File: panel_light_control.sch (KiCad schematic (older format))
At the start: 77 parts, among them J1 Conn_01x02, J6 Conn_01x04, Q1 IRF540N, Q2 IRF540N, Q3 IRF540N, U1 L7805, U2 LM324

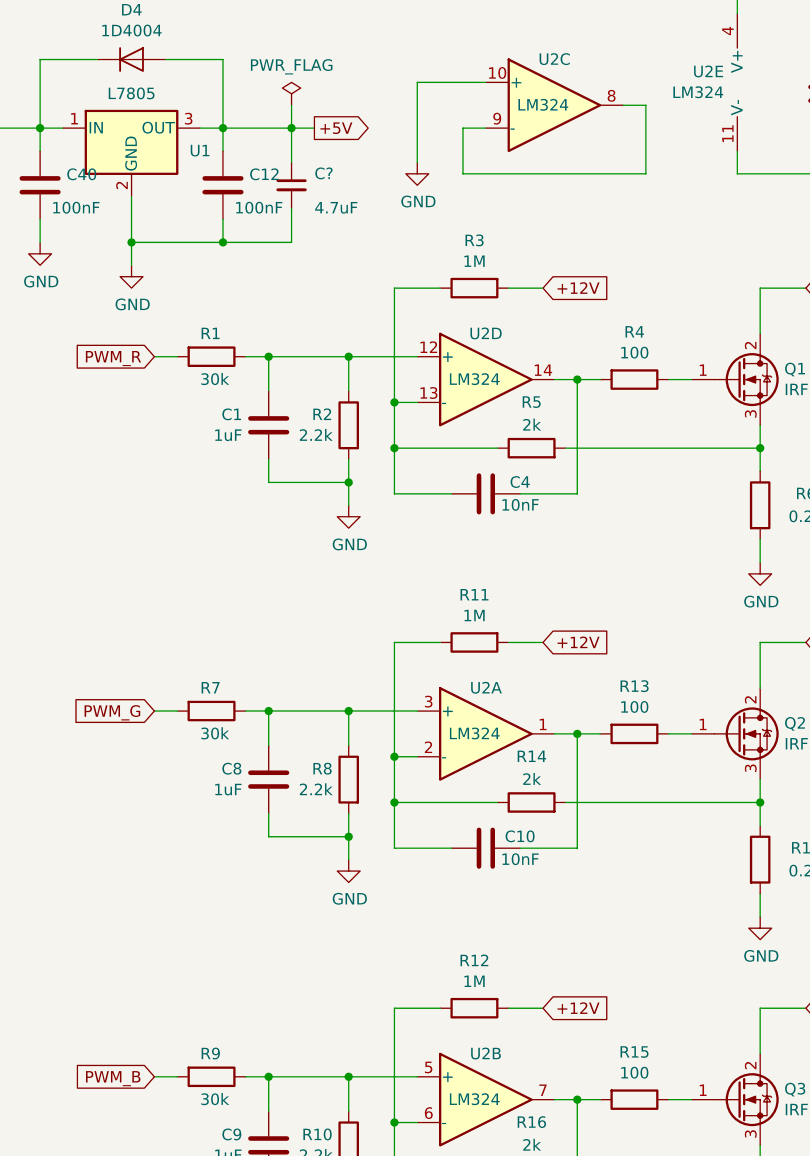
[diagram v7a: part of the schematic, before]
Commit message: added BOM info, minor tweaks to artwork
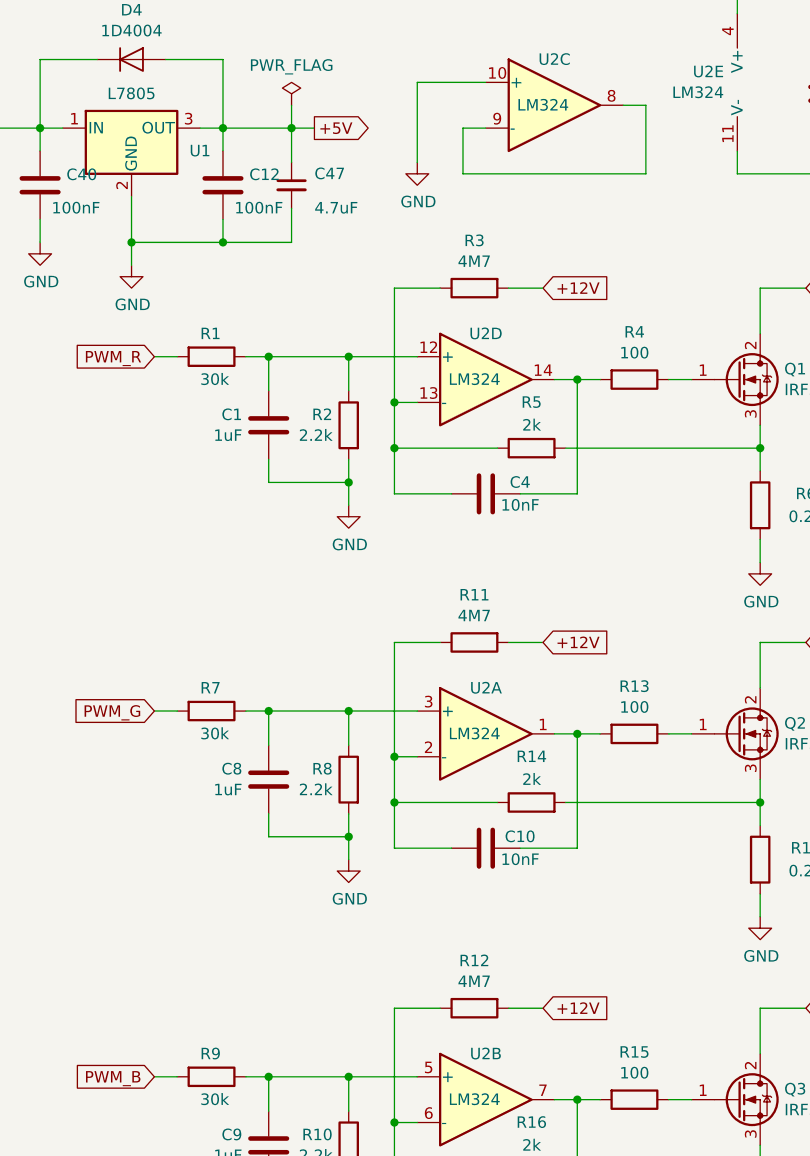
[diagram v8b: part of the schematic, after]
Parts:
- DBG1: DigiKey (none) -> 455-1723-ND‎; MPN (none) -> S6B-PH-K-S(LF)(SN)‎
- I2C1, UART1: DigiKey (none) -> 455-1721-ND‎; MPN (none) -> S4B-PH-K-S(LF)(SN)‎
- J6: DigiKey (none) -> 455-1721-ND‎; MPN (none) -> S4B-PH-K-S(LF)(SN)
- JTAG1: DigiKey (none) -> 455-1724-ND‎; MPN (none) -> S7B-PH-K-S(LF)(SN)‎
- PANEL1, PANEL2: MPN (none) -> PJ-063AH; Mouser (none) -> 490-PJ-063AH
- PS1, PS2: Mouser (none) -> 709-LDD-1000H
- Q1, Q2, Q3: MPN (none) -> IRF540NPBF; Mouser (none) -> 942-IRF540NPBF
- R11, R12, R3: value 1M -> 4M7
- R17, R18, R6: MPN (none) -> RL1220S-R22-F; Mouser (none) -> 754-RL1220S-R22-F
- SPI0: DigiKey (none) -> 455-1727-ND‎; MPN (none) -> S10B-PH-K-S(LF)(SN)‎
- SPI1: DigiKey (none) -> 455-1724-ND‎; MPN (none) -> S7B-PH-K-S(LF)(SN)
- gave numbers to parts that had none: 1
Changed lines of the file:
@@
 F 12 "LDD-1000H" H 2750 5850 50  0001 L CNN "Arrow Part Number"
 F 13 "" H 2750 5750 50  0001 L CNN "Arrow Price/Stock"
+F 14 "709-LDD-1000H" H 1500 6750 50  0001 C CNN "Mouser"
 	1    1500 6750
 	1    0    0    -1
@@
 F 2 "Connector_BarrelJack:BarrelJack_CUI_PJ-063AH_Horizontal" H 10600 600 50  0001 C CNN
 F 3 "~" H 10600 600 50  0001 C CNN
+F 4 "PJ-063AH " H 10600 600 50  0001 C CNN "MPN"
+F 5 "490-PJ-063AH" H 10600 600 50  0001 C CNN "Mouser"
 	1    10600 600
 	1    0    0    -1
@@
 F 2 "Connector_BarrelJack:BarrelJack_CUI_PJ-063AH_Horizontal" H 10600 1000 50  0001 C CNN
 F 3 "~" H 10600 1000 50  0001 C CNN
+F 4 "PJ-063AH " H 10600 1000 50  0001 C CNN "MPN"
+F 5 "490-PJ-063AH " H 10600 1000 50  0001 C CNN "Mouser"
 	1    10600 1000
 	1    0    0    -1
@@
 F 8 "http://www.alliedelec.com/mean-well-usa-ldd-1000h/70345763/" H 2750 4800 50  0001 L CNN "Allied Price/Stock"
 F 9 "LDD-1000H" H 2750 4700 50  0001 L CNN "Arrow Part Number"
+F 10 "709-LDD-1000H" H 1500 5600 50  0001 C CNN "Mouser"
 	1    1500 5600
 	1    0    0    -1
@@
 F 2 "Connector_JST:JST_PH_S4B-PH-K_1x04_P2.00mm_Horizontal" H 10600 4250 50  0001 C CNN
 F 3 "~" H 10600 4250 50  0001 C CNN
+F 4 "S4B-PH-K-S(LF)(SN)‎" H 10600 4250 50  0001 C CNN "MPN"
+F 5 "455-1721-ND‎" H 10600 4250 50  0001 C CNN "DigiKey"
 	1    10600 4250
 	1    0    0    -1
@@
 F 2 "Connector_JST:JST_PH_S6B-PH-K_1x06_P2.00mm_Horizontal" H 10600 3050 50  0001 C CNN
 F 3 "~" H 10600 3050 50  0001 C CNN
+F 4 "S6B-PH-K-S(LF)(SN)‎ " H 10600 3050 50  0001 C CNN "MPN"
+F 5 "455-1723-ND‎" H 10600 3050 50  0001 C CNN "DigiKey"
 	1    10600 3050
 	1    0    0    -1
@@
 F 2 "Resistor_SMD:R_1206_3216Metric" V 8130 4400 50  0001 C CNN
 F 3 "~" H 8200 4400 50  0001 C CNN
+F 4 "RL1220S-R22-F" H 8200 4400 50  0001 C CNN "MPN"
+F 5 "754-RL1220S-R22-F" H 8200 4400 50  0001 C CNN "Mouser"
 	1    8200 4400
 	1    0    0    -1
@@
 F 2 "Package_TO_SOT_THT:TO-220-3_Vertical" H 8350 3775 50  0001 L CIN
 F 3 "http://www.irf.com/product-info/datasheets/data/irf540n.pdf" H 8100 3850 50  0001 L CNN
+F 4 "IRF540NPBF" H 8100 3850 50  0001 C CNN "MPN"
+F 5 "942-IRF540NPBF" H 8100 3850 50  0001 C CNN "Mouser"
 	1    8100 3850
 	1    0    0    -1
@@
 P 6950 3450
 F 0 "R11" V 6743 3450 50  0000 C CNN
-F 1 "1M" V 6834 3450 50  0000 C CNN
+F 1 "4M7" V 6834 3450 50  0000 C CNN
 F 2 "Resistor_SMD:R_0603_1608Metric" V 6880 3450 50  0001 C CNN
 F 3 "~" H 6950 3450 50  0001 C CNN
@@
 F 2 "TerminalBlock_Phoenix:TerminalBlock_Phoenix_MKDS-1,5-4_1x04_P5.00mm_Horizontal" H 10600 1500 50  0001 C CNN
 F 3 "~" H 10600 1500 50  0001 C CNN
+F 4 "S4B-PH-K-S(LF)(SN)" H 10600 1500 50  0001 C CNN "MPN"
+F 5 "455-1721-ND‎" H 10600 1500 50  0001 C CNN "DigiKey"
 	1    10600 1500
 	1    0    0    -1
@@
 F 2 "Connector_JST:JST_PH_S4B-PH-K_1x04_P2.00mm_Horizontal" H 10600 3700 50  0001 C CNN
 F 3 "~" H 10600 3700 50  0001 C CNN
+F 4 "S4B-PH-K-S(LF)(SN)‎ " H 10600 3700 50  0001 C CNN "MPN"
+F 5 "455-1721-ND‎" H 10600 3700 50  0001 C CNN "DigiKey"
 	1    10600 3700
 	1    0    0    -1
@@
 F 2 "Connector_JST:JST_PH_S10B-PH-K_1x10_P2.00mm_Horizontal" H 10600 5100 50  0001 C CNN
 F 3 "~" H 10600 5100 50  0001 C CNN
+F 4 "S10B-PH-K-S(LF)(SN)‎ " H 10600 5100 50  0001 C CNN "MPN"
+F 5 "455-1727-ND‎" H 10600 5100 50  0001 C CNN "DigiKey"
 	1    10600 5100
 	1    0    0    -1
@@
 F 2 "Connector_JST:JST_PH_S7B-PH-K_1x07_P2.00mm_Horizontal" H 10600 2250 50  0001 C CNN
 F 3 "~" H 10600 2250 50  0001 C CNN
+F 4 "S7B-PH-K-S(LF)(SN)‎ " H 10600 2250 50  0001 C CNN "MPN"
+F 5 "455-1724-ND‎" H 10600 2250 50  0001 C CNN "DigiKey"
 	1    10600 2250
 	1    0    0    -1
@@
 F 2 "Connector_JST:JST_PH_S7B-PH-K_1x07_P2.00mm_Horizontal" H 10600 6150 50  0001 C CNN
 F 3 "~" H 10600 6150 50  0001 C CNN
+F 4 "S7B-PH-K-S(LF)(SN)" H 10600 6150 50  0001 C CNN "MPN"
+F 5 "455-1724-ND‎" H 10600 6150 50  0001 C CNN "DigiKey"
 	1    10600 6150
 	1    0    0    -1
@@
 F 2 "Resistor_SMD:R_1206_3216Metric" V 8130 6000 50  0001 C CNN
 F 3 "~" H 8200 6000 50  0001 C CNN
+F 4 "RL1220S-R22-F" H 8200 6000 50  0001 C CNN "MPN"
+F 5 "754-RL1220S-R22-F" H 8200 6000 50  0001 C CNN "Mouser"
 	1    8200 6000
 	1    0    0    -1
@@
 F 2 "Package_TO_SOT_THT:TO-220-3_Vertical" H 8350 5375 50  0001 L CIN
 F 3 "http://www.irf.com/product-info/datasheets/data/irf540n.pdf" H 8100 5450 50  0001 L CNN
+F 4 "IRF540NPBF" H 8100 5450 50  0001 C CNN "MPN"
+F 5 "942-IRF540NPBF" H 8100 5450 50  0001 C CNN "Mouser"
 	1    8100 5450
 	1    0    0    -1
@@
 P 6950 5050
 F 0 "R12" V 6743 5050 50  0000 C CNN
-F 1 "1M" V 6834 5050 50  0000 C CNN
+F 1 "4M7" V 6834 5050 50  0000 C CNN
 F 2 "Resistor_SMD:R_0603_1608Metric" V 6880 5050 50  0001 C CNN
 F 3 "~" H 6950 5050 50  0001 C CNN
@@
 F 2 "Resistor_SMD:R_1206_3216Metric" V 8130 2850 50  0001 C CNN
 F 3 "~" H 8200 2850 50  0001 C CNN
+F 4 "RL1220S-R22-F" H 8200 2850 50  0001 C CNN "MPN"
+F 5 "754-RL1220S-R22-F" H 8200 2850 50  0001 C CNN "Mouser"
 	1    8200 2850
 	1    0    0    -1
@@
 F 2 "Package_TO_SOT_THT:TO-220-3_Vertical" H 8350 2225 50  0001 L CIN
 F 3 "http://www.irf.com/product-info/datasheets/data/irf540n.pdf" H 8100 2300 50  0001 L CNN
+F 4 "IRF540NPBF" H 8100 2300 50  0001 C CNN "MPN"
+F 5 "942-IRF540NPBF" H 8100 2300 50  0001 C CNN "Mouser"
 	1    8100 2300
 	1    0    0    -1
@@
 P 6950 1900
 F 0 "R3" V 6743 1900 50  0000 C CNN
-F 1 "1M" V 6834 1900 50  0000 C CNN
+F 1 "4M7" V 6834 1900 50  0000 C CNN
 F 2 "Resistor_SMD:R_0603_1608Metric" V 6880 1900 50  0001 C CNN
 F 3 "~" H 6950 1900 50  0001 C CNN
@@
 AR Path="/5C211DD3/5BF468BF" Ref="C?"  Part="1"
 AR Path="/5C211FC6/5BF468BF" Ref="C?"  Part="1"
-F 0 "C?" H 6050 1500 50  0000 R CNN
+AR Path="/5BF468BF" Ref="C47"  Part="1"
+F 0 "C47" H 6050 1500 50  0000 R CNN
 F 1 "4.7uF" H 6050 1350 50  0000 R CNN
 F 2 "Capacitor_SMD:C_0805_2012Metric" H 6150 1450 50  0001 C CNN
